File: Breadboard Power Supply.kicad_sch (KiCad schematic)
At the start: 28 parts, among them J1 USB-C, J10 Conn_01x02_Male, J11 Conn_01x02_Male, J2 Conn_02x03_Odd_Even, J3 Conn_02x03_Odd_Even, J8 Conn_01x02_Male, J9 Conn_01x02_Male, U1 LM1117-1.8, U2 LM1117-3.3

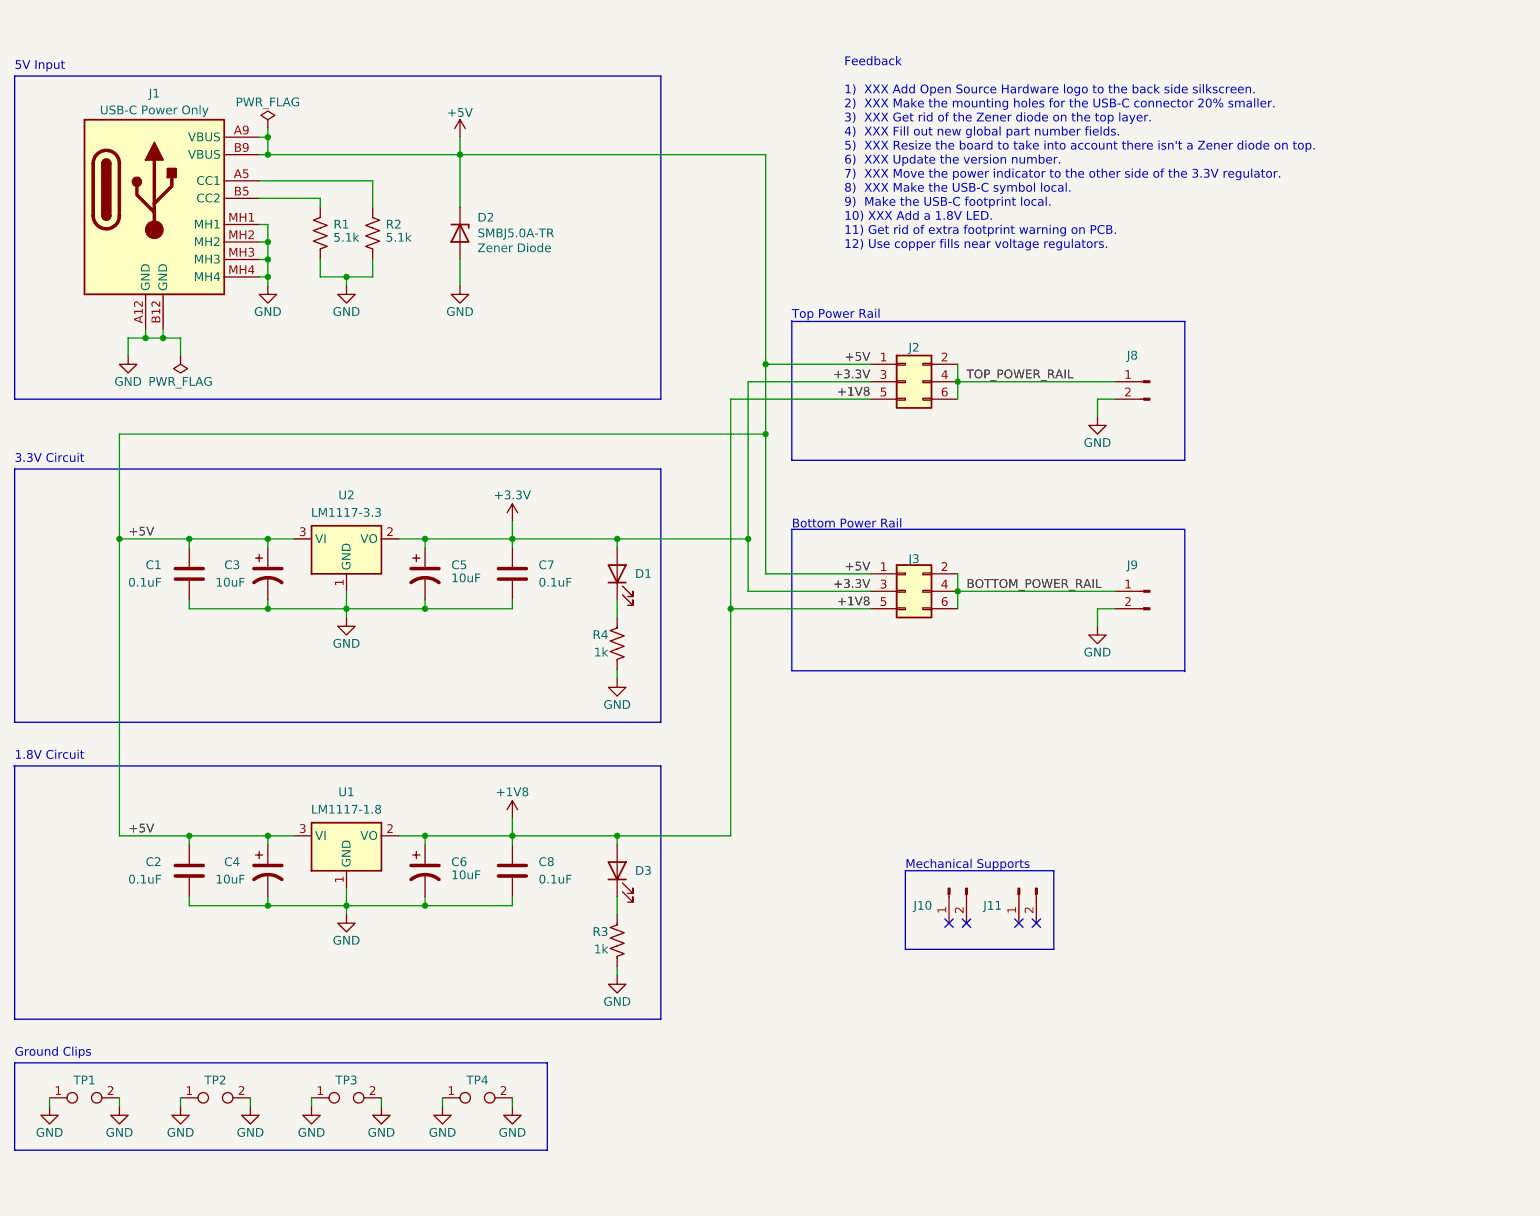
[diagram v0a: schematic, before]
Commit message: Added a symbol for the OSHW logo.
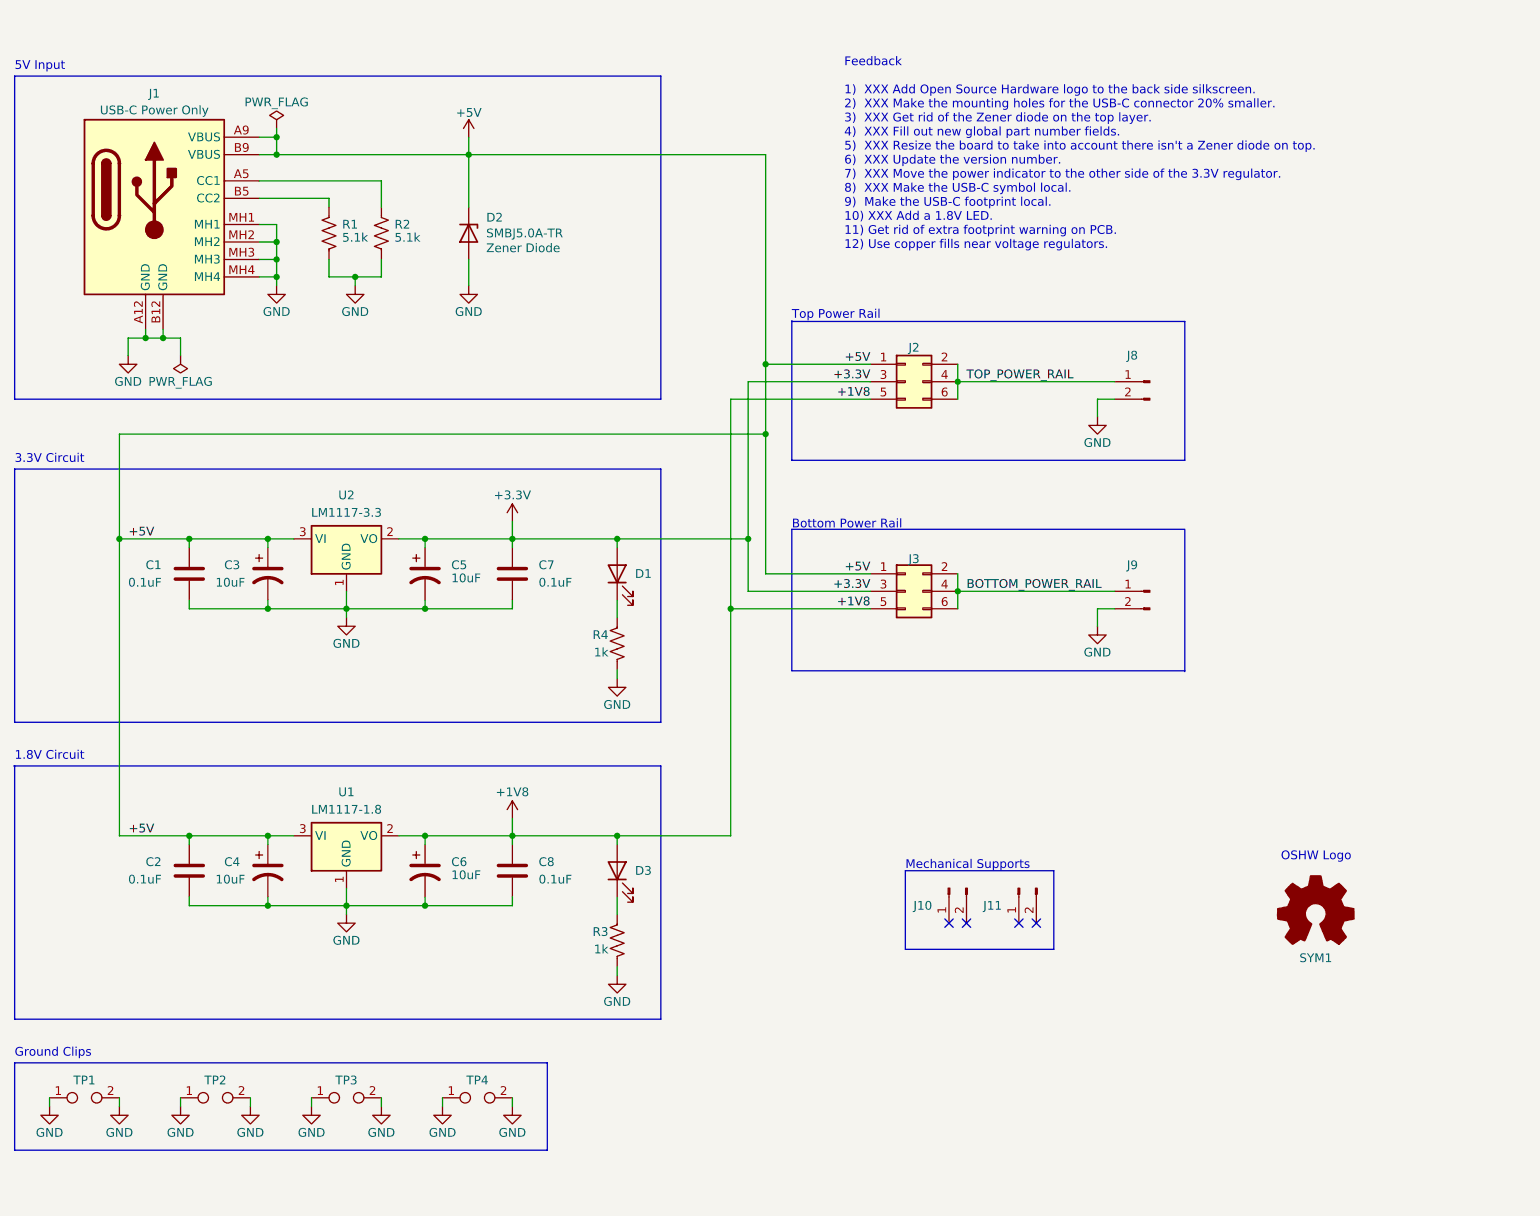
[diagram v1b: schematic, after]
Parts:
- added SYM1: Logo_Open_Hardware_Small, Symbol:OSHW-Logo_5.7x6mm_SilkScreen, symbol Graphic:Logo_Open_Hardware_Small
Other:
- note added: "OSHW Logo"
- moved on the sheet: D2, R1, R2

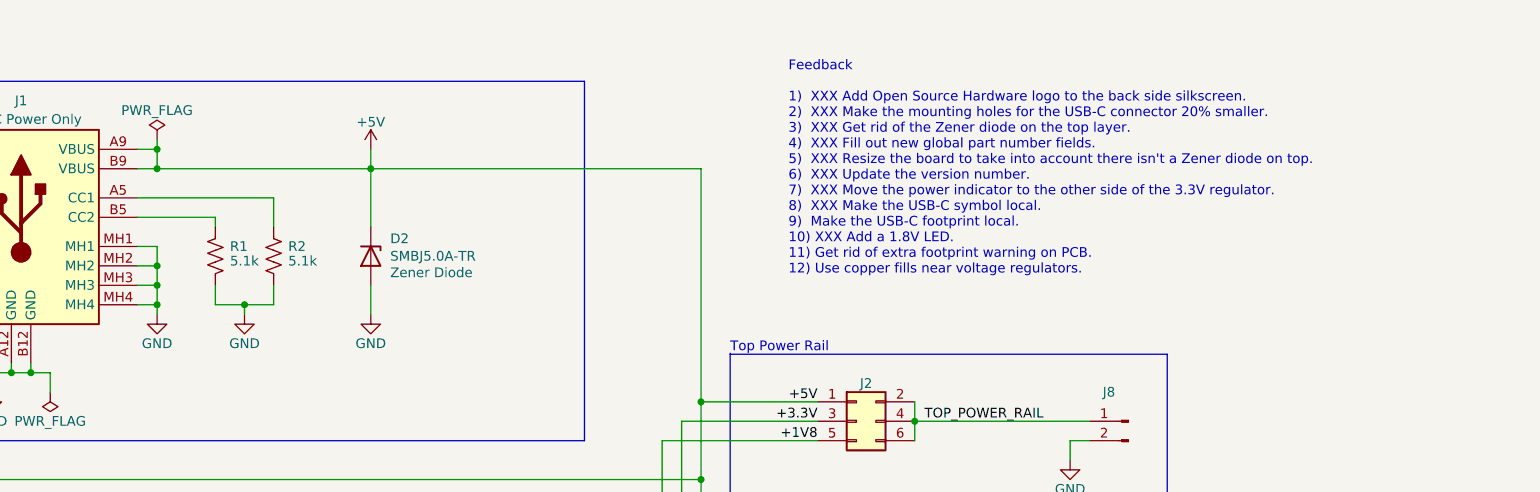
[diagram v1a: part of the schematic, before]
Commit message: Moved the USB-C to the local footprints library.
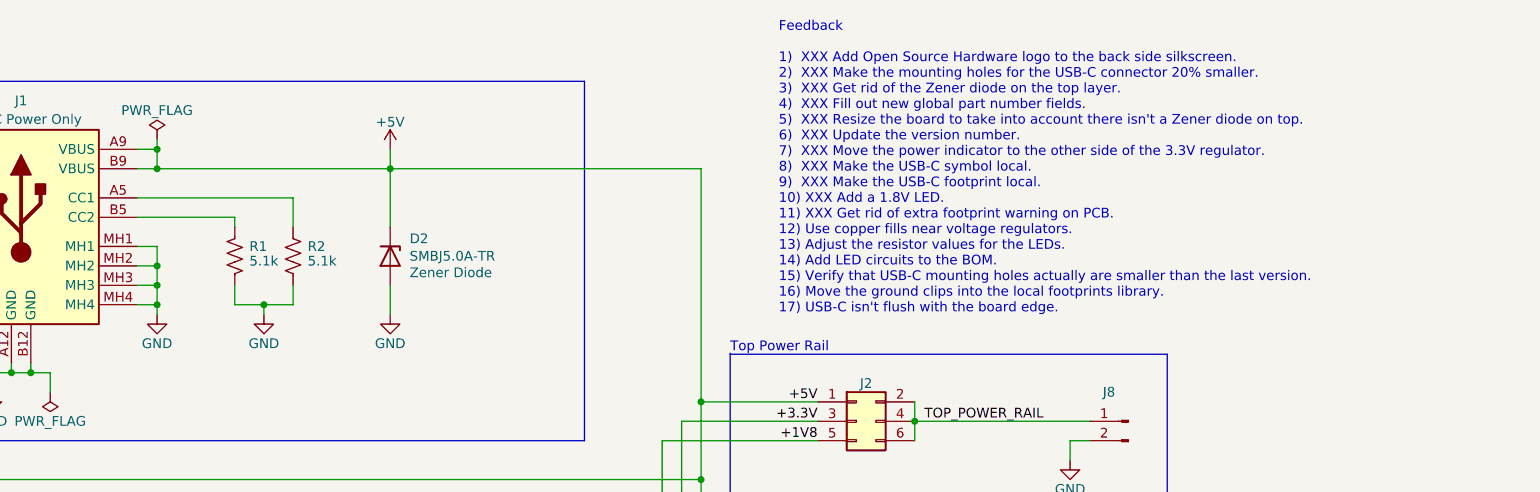
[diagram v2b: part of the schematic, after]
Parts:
- J1: footprint My-Global-Footprints:USB-C Surface Mount -> My-Local-Footprints:USB-C Power Only
- TP1, TP2, TP3, TP4: footprint My-Global-Footprints:Keystone 1430-1 -> My-Local-Footprints:Keystone 1430-1
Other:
- moved on the sheet: D2, R1, R2

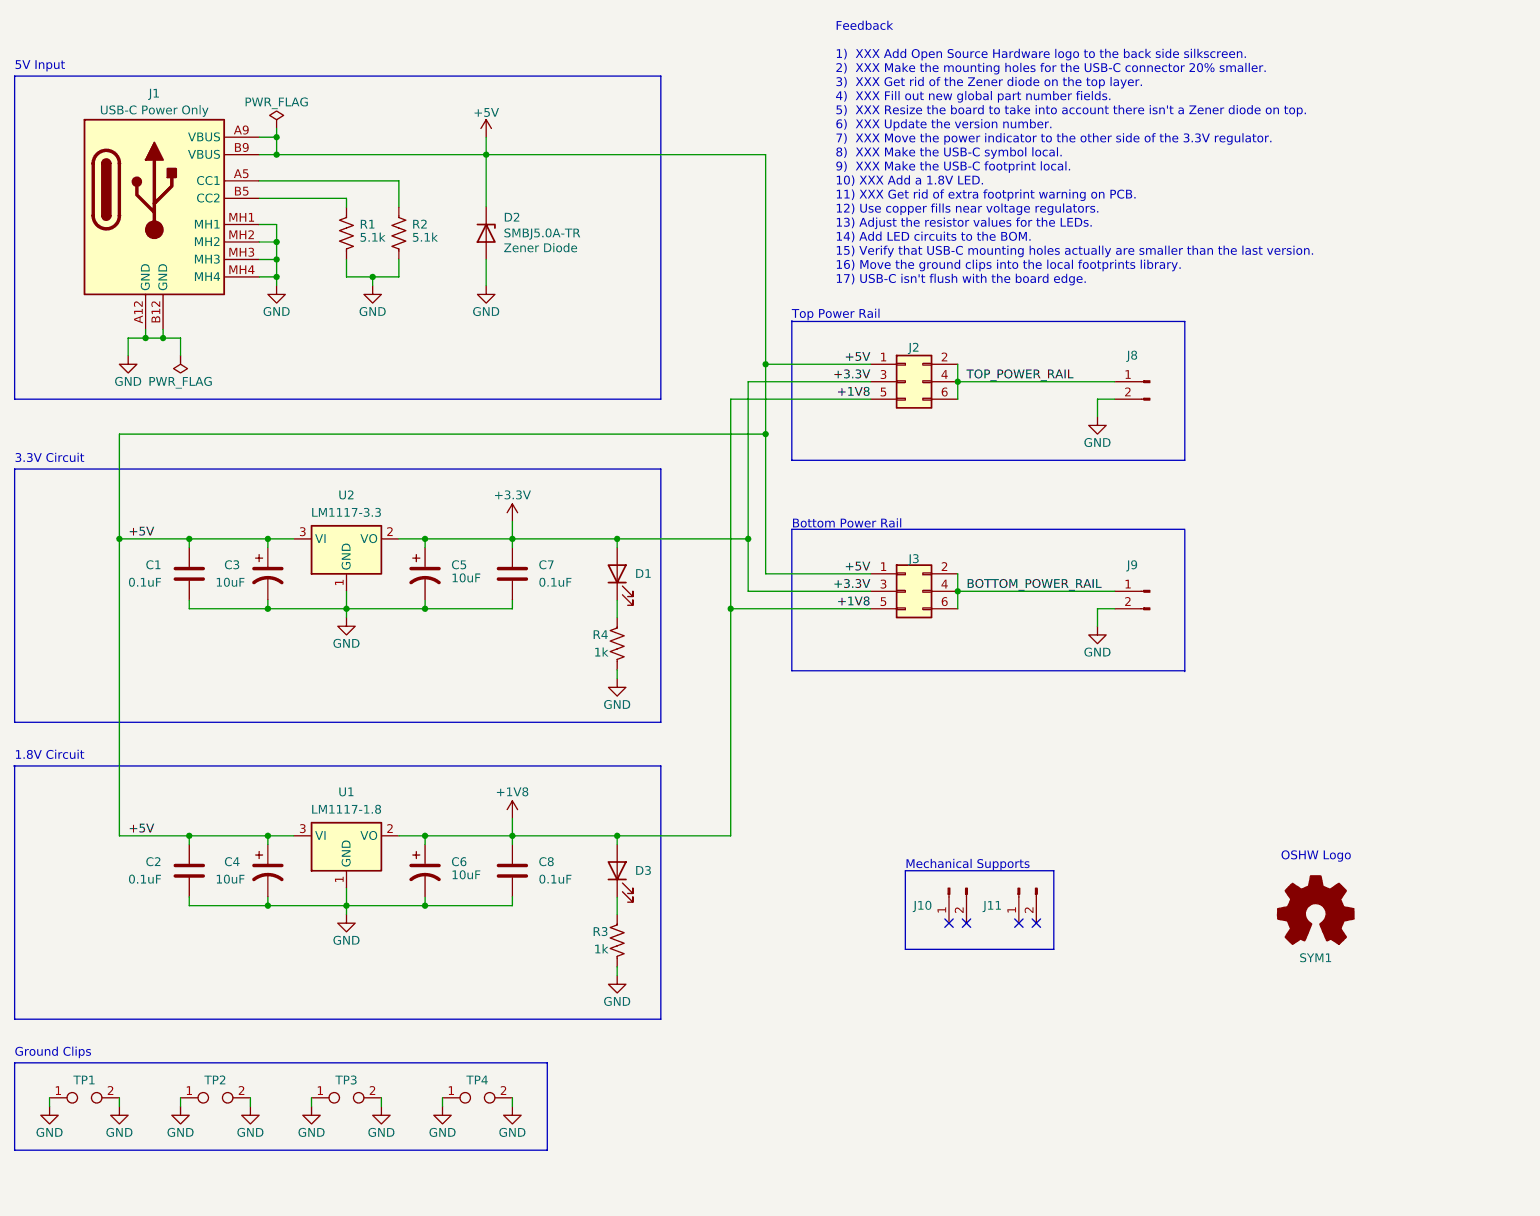
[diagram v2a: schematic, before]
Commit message: Updated BOM.
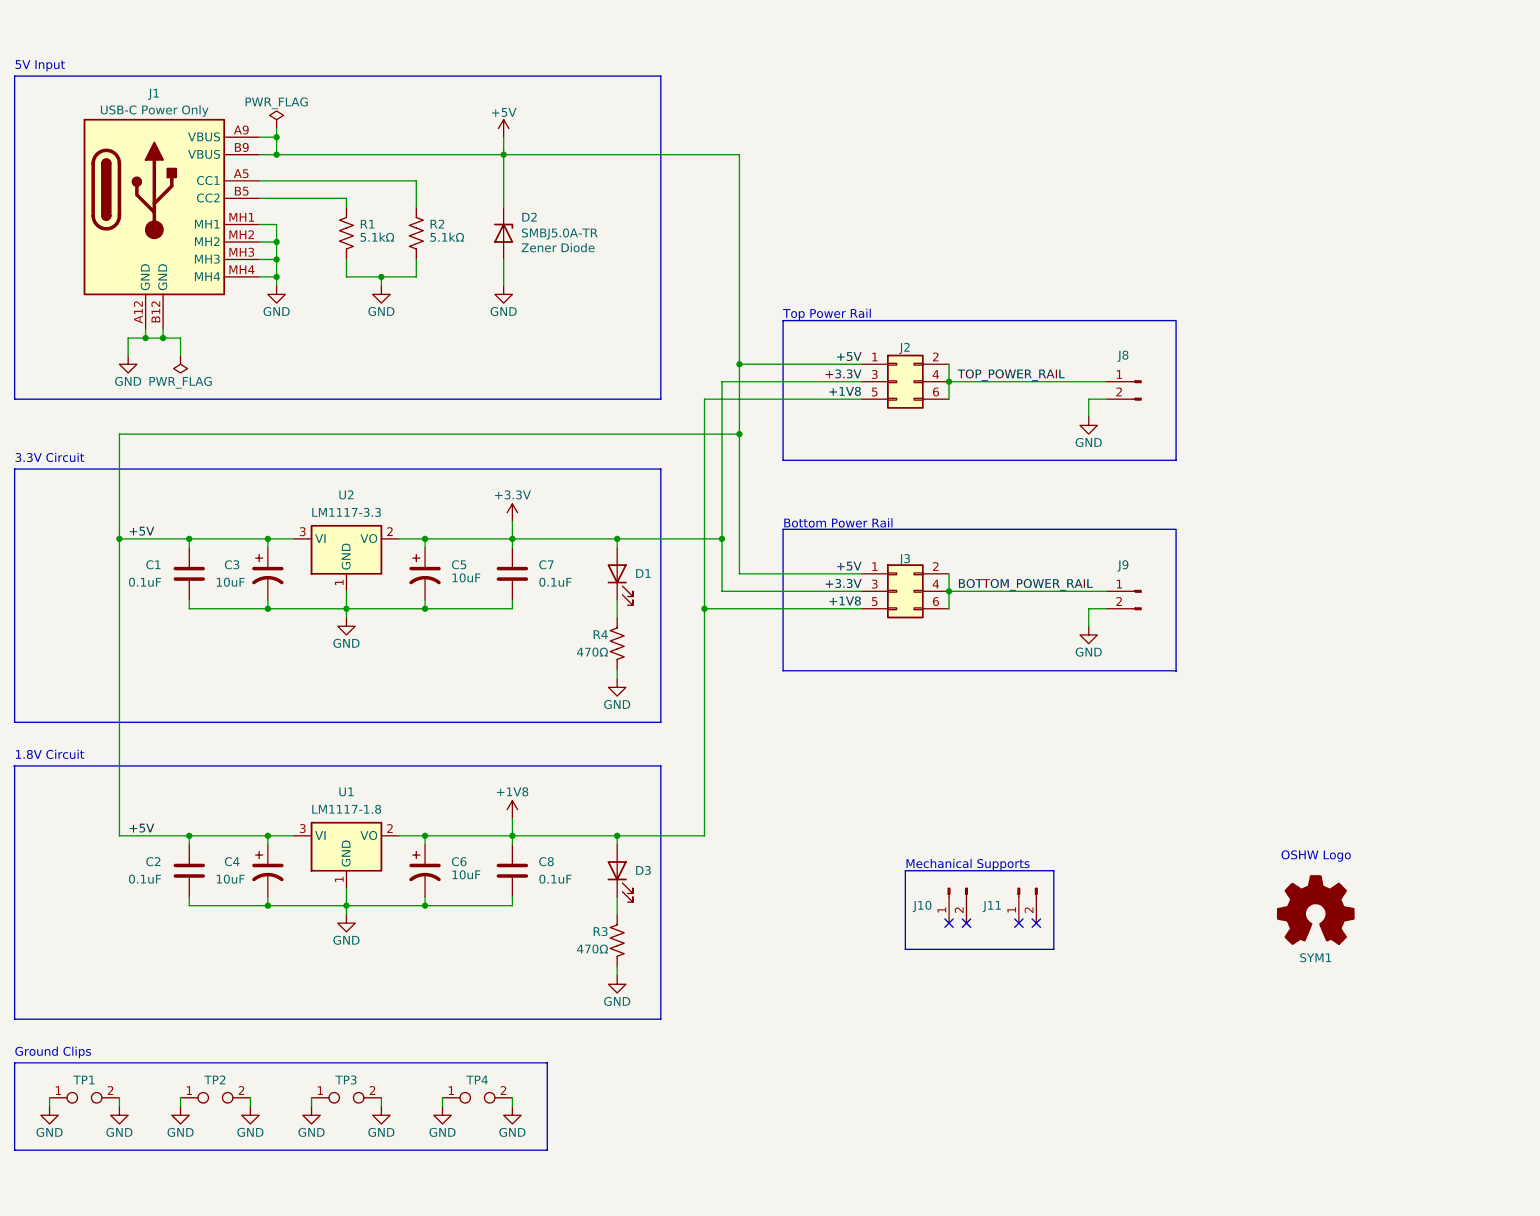
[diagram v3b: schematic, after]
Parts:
- R1, R2: value 5.1k -> 5.1kΩ
- R3: value 1k -> 470Ω
- R4: value 1k -> 470Ω
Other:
- note removed: "Feedback 1) XXX Add Open Source Hardware logo to the back side silkscreen. 2) XXX Make the mounting holes for the USB-C connector 20% smaller. 3) XXX Get rid of the Zener diode on the top layer. 4) XXX Fill out new global part number fields. 5) XXX Resize the board to take into account there isn't a Zener diode on top. 6) XXX Update the version number. 7) XXX Move the power indicator to the other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"
- moved on the sheet: D2, J2, J3, J8, J9, R2

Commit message: Version 7
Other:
- note added: "Feedback 1) The middle bottom outline cuts the trace."
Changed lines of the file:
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@@
+    (effects (font (size 1.27 1.27)) (justify left bottom))
+  )
+  (text "Feedback\n\n1) The middle bottom outline cuts the trace."
+    (at 177.8 25.4 0)
     (effects (font (size 1.27 1.27)) (justify left bottom))
   )

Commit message: Added feedback.
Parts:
- R3: value 470Ω -> 220Ω
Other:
- note added: "Feedback 1) The middle bottom outline cuts the trace. 2) Make github.com/tstills 0.8mm high. 3) Take the USB pins out out of the solder stencil. 4) Make the USB-C mounting holes 15% smaller. 5) Move the C8 reference designator to the middle of the cap. 6) Move the C5 reference designator up a bit. 7) Get rid of the dot on the USB silkscreen. 8) Move the J1 reference designator to the bottom of th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"
- note removed: "Feedback 1) The middle bottom outline cuts the trace."
- moved on the sheet: C1, C2, C3, C4, C5, C6, C7, C8, D1, D3, R3, R4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

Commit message: Added feedback.
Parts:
- R3: value 220Ω -> 150Ω
- R4: value 470Ω -> 330Ω
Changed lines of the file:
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@@
     (effects (font (size 1.27 1.27)) (justify left bottom))
   )
-  (text "Feedback\n\n1)  The middle bottom outline cuts the trace.\n2)  Make github.com/tstills 0.8mm high.\n3)  Take the USB pins out out of the solder stencil.\n4)  Make the USB-C mounting holes 15% smaller.\n5)  Move the C8 reference designator to the middle of the cap.\n6)  Move the C5 reference designator up a bit.\n7)  Get rid of the dot on the USB silkscreen.\n8)  Move the J1 reference designator to the bottom of the USB-C.\n9)  Move the 10uF caps down a bit so the reference designators are above and below.\n10) Update version numbers."
+  (text "Feedback\n\n1)  The middle bottom outline cuts the trace.\n2)  Make github.com/tstills 0.8mm high.\n3)  Take the USB pins out out of the solder stencil.\n4)  Make the USB-C mounting holes 15% smaller.\n5)  Move the C8 reference designator to the middle of the cap.\n6)  Move the C5 reference designator up a bit.\n7)  Get rid of the dot on the USB silkscreen.\n8)  Move the J1 reference designator to the bottom of the USB-C.\n9)  Move the 10uF caps down a bit so the reference designators are above and below.\n10) Update version numbers.\n11) Have a single LED."
     (at 177.8 41.91 0)
     (effects (font (size 1.27 1.27)) (justify left bottom))
@@
       (effects (font (size 1.27 1.27)) (justify left))
     )
-    (property "Value" "220Ω" (at 144.78 109.22 0)
+    (property "Value" "150Ω" (at 144.78 109.22 0)
       (effects (font (size 1.27 1.27)) (justify left))
     )
@@
       (effects (font (size 1.27 1.27)) (justify left))
     )
-    (property "Value" "470Ω" (at 144.78 157.48 0)
-      (effects (font (size 1.27 1.27)) (justify left))
-    )
+    (property "Value" "330Ω" (at 144.78 157.48 0)
+      (effects (font (size 1.27 1.27)) (justify left))
+    )
